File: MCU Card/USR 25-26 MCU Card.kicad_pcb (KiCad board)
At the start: 2 copper layers, 14 parts

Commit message: Update MCU card layout
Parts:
- removed D5, D6: LED, LED_SMD:LED_1206_3216Metric_Pad1.42x1.75mm_HandSolder
- removed R4, R5, R6: 220, Resistor_SMD:R_1206_3216Metric_Pad1.30x1.75mm_HandSolder
- added A2: RaspberryPi_Pico_W, Module:RaspberryPi_Pico_Common_THT, F.Cu at (119.4, 78.6)
- added U1: ~, USR:LSM6DSO, F.Cu at (161.7, 128.0)
- A1: footprint Module:RaspberryPi_Pico_W_SMD_HandSolder -> Module:RaspberryPi_Pico_Common_THT
- D1, D2, D3: footprint LED_SMD:LED_1206_3216Metric_Pad1.42x1.75mm_HandSolder -> LED_THT:LED_D3.0mm
- D4: value LED -> 1N5819; footprint LED_SMD:LED_1206_3216Metric_Pad1.42x1.75mm_HandSolder -> Diode_THT:D_DO-41_SOD81_P10.16mm_Horizontal
- R1, R2, R3: value 220 -> 510R; footprint Resistor_SMD:R_1206_3216Metric_Pad1.30x1.75mm_HandSolder -> Resistor_THT:R_Axial_DIN0207_L6.3mm_D2.5mm_P10.16mm_Horizontal
- moved J1 100.2 mm to (138.4, 144.6)
- moved D1 78.5 mm to (168.9, 101.4), turned to 90 degrees
- moved D2 70.6 mm to (168.9, 91.3), turned to 90 degrees
- moved D3 62.1 mm to (168.9, 81.1), turned to 90 degrees
- moved R1 51.8 mm to (152.4, 98.9)
- moved R2 39.7 mm to (152.4, 88.7)
- moved A1 29.9 mm to (61.0, 78.7)
- moved R3 28.7 mm to (152.4, 78.6)
- moved D4 23.8 mm to (88.9, 81.1)
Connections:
- A1 pad 1: Net-(A1-GPIO0) -> unconnected-(A1-GPIO0-Pad1)
- A1 pad 11: Net-(A1-GPIO8) -> unconnected-(A1-GPIO8-Pad11)
- A1 pad 21: Net-(A1-GPIO16) -> unconnected-(A1-GPIO16-Pad21)
- A1 pad 22: /SPI0_CS2 -> unconnected-(A1-GPIO17-Pad22)
- A1 pad 24: /M1_SLP -> unconnected-(A1-GPIO18-Pad24)
- A1 pad 25: /M2_SLP -> unconnected-(A1-GPIO19-Pad25)
- A1 pad 26: /M1_FLT -> unconnected-(A1-GPIO20-Pad26)
- A1 pad 27: /M2_FLT -> unconnected-(A1-GPIO21-Pad27)
- A1 pad 29: Net-(A1-GPIO22) -> unconnected-(A1-GPIO22-Pad29)
- A1 pad 39: +5V -> Net-(A1-VSYS)
- A1 pad 40: unconnected-(A1-VBUS-Pad40) -> VBUS
- D1 pad 1: Net-(D1-K) -> GND
- D1 pad 2: +5V -> Net-(D1-A)
- D2 pad 1: Net-(D2-K) -> GND
- D2 pad 2: +3V3 -> Net-(D2-A)
- D3 pad 1: Net-(D3-K) -> GND
- D3 pad 2: Net-(A1-GPIO0) -> Net-(D3-A)
- D4 pad 1: Net-(D4-K) -> Net-(A1-VSYS)
- D4 pad 2: Net-(A1-GPIO8) -> +5V
- J1 pad 32: +5V -> unconnected-(J1-Pad32)
- J1 pad 33: +3V3 -> unconnected-(J1-Pad33)
- J1 pad 34: GND -> unconnected-(J1-Pad34)
- J1 pad 35: /SPI0_MOSI -> unconnected-(J1-Pad35)
- J1 pad 36: /SPI0_MISO -> unconnected-(J1-Pad36)
- J1 pad 37: /SPI0_SCLK -> unconnected-(J1-Pad37)
- J1 pad 38: /SPI0_CS0 -> unconnected-(J1-Pad38)
- J1 pad 39: /SPI0_CS1 -> unconnected-(J1-Pad39)
- J1 pad 40: /SPI0_CS2 -> unconnected-(J1-Pad40)
- J1 pad 41: GND -> unconnected-(J1-Pad41)
- J1 pad 42: /SPI1_MOSI -> unconnected-(J1-Pad42)
- J1 pad 43: /SPI1_MISO -> unconnected-(J1-Pad43)
- J1 pad 44: /SPI1_SCLK -> unconnected-(J1-Pad44)
- J1 pad 45: /SPI1_CS0 -> unconnected-(J1-Pad45)
- J1 pad 46: /SPI1_CS1 -> unconnected-(J1-Pad46)
- J1 pad 47: GND -> unconnected-(J1-Pad47)
- J1 pad 48: /M1_DIR -> unconnected-(J1-Pad48)
- J1 pad 49: /M1_FLT -> unconnected-(J1-Pad49)
- J1 pad 50: /M1_PWM -> unconnected-(J1-Pad50)
- J1 pad 51: /M1_SLP -> unconnected-(J1-Pad51)
- J1 pad 52: GND -> unconnected-(J1-Pad52)
- J1 pad 53: /M2_DIR -> unconnected-(J1-Pad53)
- J1 pad 54: /M2_FLT -> unconnected-(J1-Pad54)
- J1 pad 55: /M2_PWM -> unconnected-(J1-Pad55)
- J1 pad 56: /M2_SLP -> unconnected-(J1-Pad56)
- R1 pad 1: Net-(D1-K) -> VBUS
- R1 pad 2: GND -> Net-(D1-A)
- R2 pad 1: Net-(D2-K) -> +5V
- R2 pad 2: GND -> Net-(D2-A)
- R3 pad 1: Net-(D6-K) -> +3V3
- R3 pad 2: GND -> Net-(D3-A)
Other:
- board outline added: 129.5 x 76.2 mm
- board text added: "3V3_OUT"
- board text added: ":)"
- board text added: "JG Vincent Banh MCU Card 25-26"
- board text added: "SEC_PWR"
- board text added: "USB_PWR"

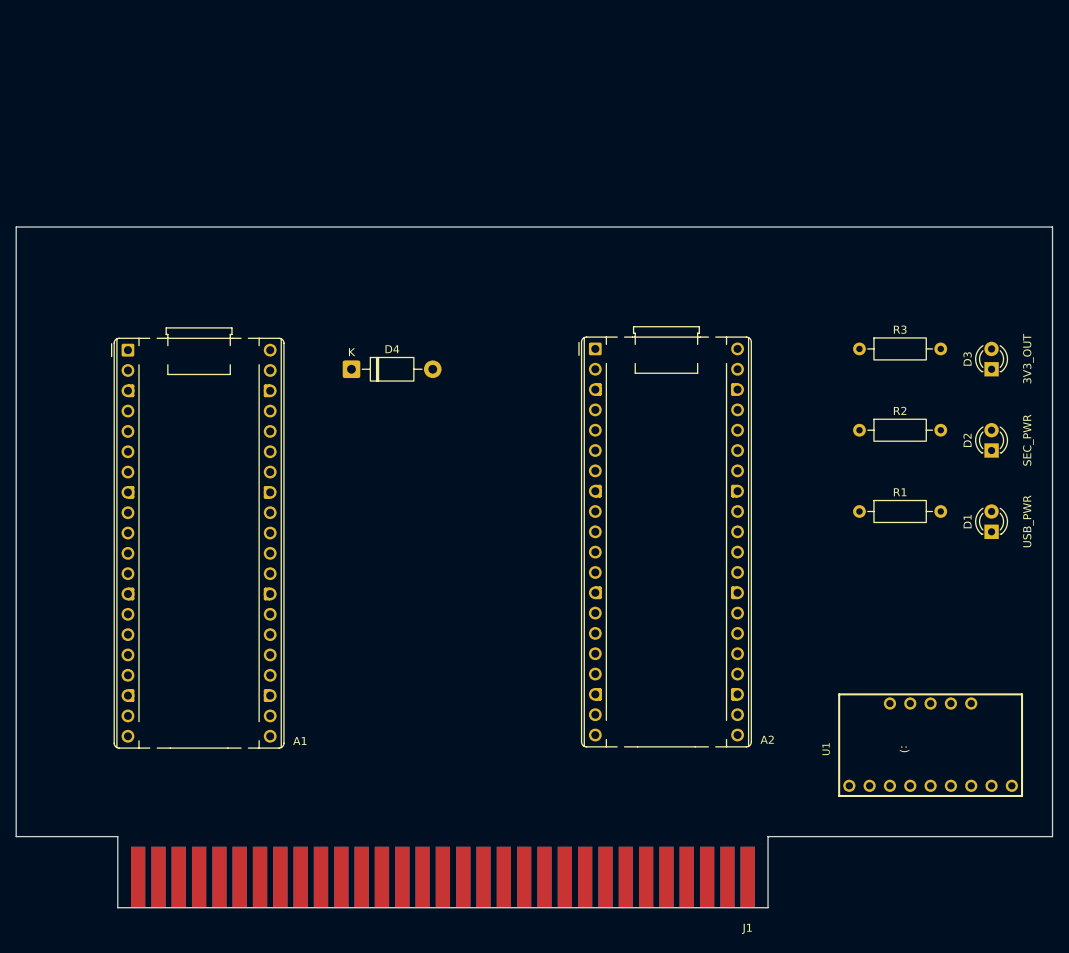
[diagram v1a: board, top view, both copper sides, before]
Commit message: updated MCU card
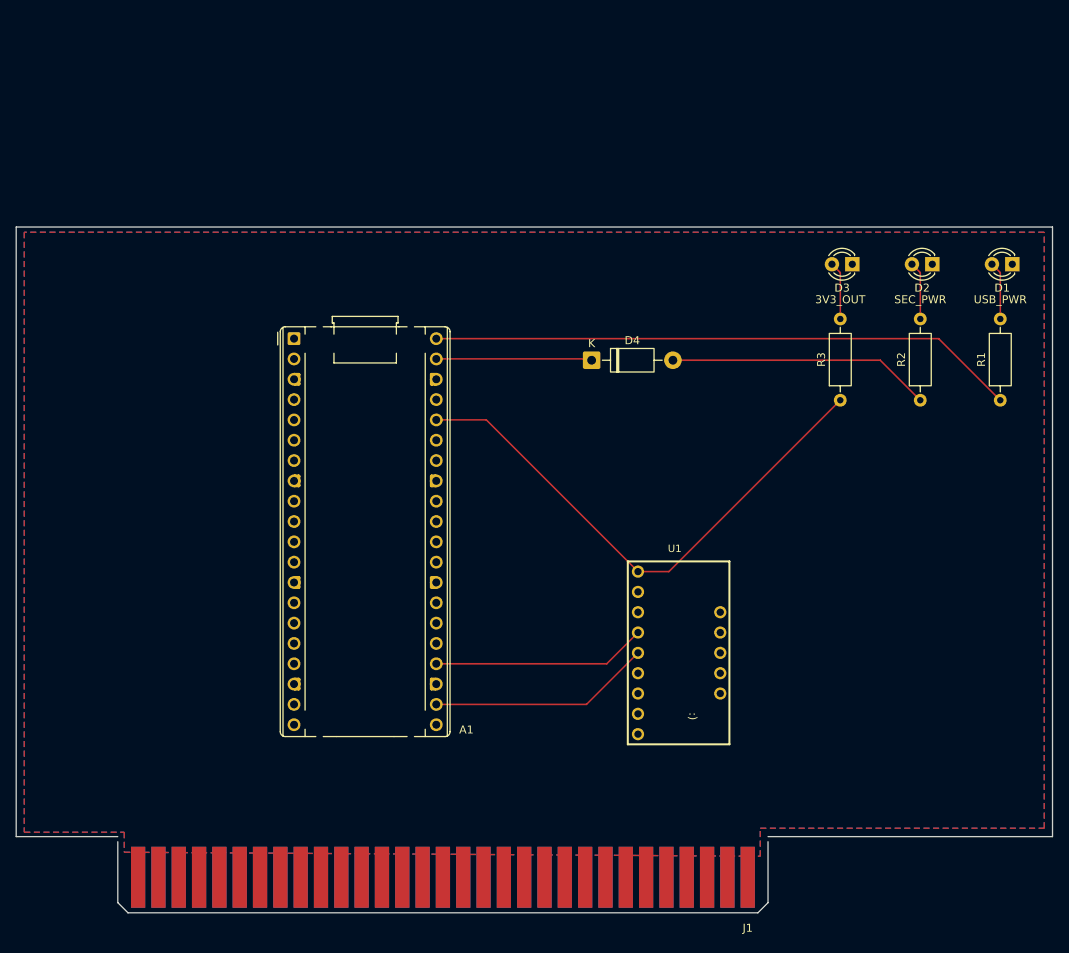
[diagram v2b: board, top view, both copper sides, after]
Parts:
- removed A2: RaspberryPi_Pico_W, Module:RaspberryPi_Pico_Common_THT
- moved U1 33.6 mm to (129.9, 117.0), turned to 0 degrees
- moved D1 33.5 mm to (171.5, 68.0), turned to 180 degrees
- moved D4 30.0 mm to (118.9, 80.0)
- moved D2 24.4 mm to (161.5, 68.0), turned to 180 degrees
- moved R1 22.4 mm to (170.0, 85.0), turned to 90 degrees
- moved D3 21.8 mm to (151.5, 68.0), turned to 180 degrees
- moved A1 20.8 mm to (81.7, 77.3)
- moved R2 8.47 mm to (160.0, 85.0), turned to 90 degrees
- moved R3 6.85 mm to (150.0, 85.0), turned to 90 degrees
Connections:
- A1 pad 1: unconnected-(A1-GPIO0-Pad1) -> /M1_DIR
- A1 pad 10: /M2_DIR -> /M4_PWM
- A1 pad 11: unconnected-(A1-GPIO8-Pad11) -> /M1_SLP
- A1 pad 12: /SPI1_CS0 -> /M2_SLP
- A1 pad 14: /SPI1_SCLK -> /M3_SLP
- A1 pad 15: /SPI1_MOSI -> /M4_SLP
- A1 pad 16: /SPI1_MISO -> /UART_TX_MICRO
- A1 pad 17: /SPI1_CS1 -> /UART_RX_MICRO
- A1 pad 19: /M1_PWM -> /M1_FLT
- A1 pad 2: /SPI0_CS0 -> /M1_PWM
- A1 pad 20: /M2_PWM -> /M2_FLT
- A1 pad 21: unconnected-(A1-GPIO16-Pad21) -> /M3_FLT
- A1 pad 22: unconnected-(A1-GPIO17-Pad22) -> /IMU_SCL
- A1 pad 24: unconnected-(A1-GPIO18-Pad24) -> /IMU_SDA
- A1 pad 25: unconnected-(A1-GPIO19-Pad25) -> /M4_FLT
- A1 pad 4: /SPI0_SCLK -> /M2_DIR
- A1 pad 5: /SPI0_MOSI -> /M2_PWM
- A1 pad 6: /SPI0_MISO -> /M3_DIR
- A1 pad 7: /SPI0_CS1 -> /M3_PWM
- A1 pad 9: /M1_DIR -> /M4_DIR
- J1 pad 1: unconnected-(J1-Pad1) -> /UART_TX_MICRO
- J1 pad 10: unconnected-(J1-Pad10) -> /M1_FLT
- J1 pad 11: unconnected-(J1-Pad11) -> /M1_SLP
- J1 pad 12: unconnected-(J1-Pad12) -> GND
- J1 pad 13: unconnected-(J1-Pad13) -> /M2_DIR
- J1 pad 14: unconnected-(J1-Pad14) -> /M2_PWM
- J1 pad 15: unconnected-(J1-Pad15) -> GND
- J1 pad 16: unconnected-(J1-Pad16) -> /M2_FLT
- J1 pad 17: unconnected-(J1-Pad17) -> /M2_SLP
- J1 pad 18: unconnected-(J1-Pad18) -> GND
- J1 pad 19: unconnected-(J1-Pad19) -> /M3_DIR
- J1 pad 2: unconnected-(J1-Pad2) -> /UART_RX_MICRO
- J1 pad 20: unconnected-(J1-Pad20) -> /M3_PWM
- J1 pad 21: unconnected-(J1-Pad21) -> GND
- J1 pad 22: unconnected-(J1-Pad22) -> /M3_FLT
- J1 pad 23: unconnected-(J1-Pad23) -> /M3_SLP
- J1 pad 24: unconnected-(J1-Pad24) -> GND
- J1 pad 25: unconnected-(J1-Pad25) -> /M4_DIR
- J1 pad 26: unconnected-(J1-Pad26) -> /M4_PWM
- J1 pad 27: unconnected-(J1-Pad27) -> GND
- J1 pad 28: unconnected-(J1-Pad28) -> /M4_FLT
- J1 pad 29: unconnected-(J1-Pad29) -> /M4_SLP
- J1 pad 3: unconnected-(J1-Pad3) -> GND
- J1 pad 30: unconnected-(J1-Pad30) -> GND
- J1 pad 31: unconnected-(J1-Pad31) -> +5V
- J1 pad 34: unconnected-(J1-Pad34) -> GND
- J1 pad 39: unconnected-(J1-Pad39) -> GND
- J1 pad 6: unconnected-(J1-Pad6) -> GND
- J1 pad 7: unconnected-(J1-Pad7) -> /M1_DIR
- J1 pad 8: unconnected-(J1-Pad8) -> /M1_PWM
- J1 pad 9: unconnected-(J1-Pad9) -> GND
- U1 pad 1: unconnected-(U1-VDD3V3_out-Pad1) -> +3V3
- U1 pad 10: unconnected-(U1-GND-Pad10) -> GND
- U1 pad 11: unconnected-(U1-SDx-Pad11) -> GND
- U1 pad 12: unconnected-(U1-SCx-Pad12) -> GND
- U1 pad 4: unconnected-(U1-SDA/SDI/SDO-Pad4) -> /IMU_SDA
- U1 pad 5: unconnected-(U1-SCL/SPC-Pad5) -> /IMU_SCL
- U1 pad 6: unconnected-(U1-SDO/SA0-Pad6) -> Net-(U1-SDO/SA0)
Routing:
- net VBUS: track 0.00 -> 73.7 mm
- net +3V3: track 0.00 -> 67.2 mm
- net +5V: track 0.00 -> 33.0 mm
- net /IMU_SCL: track 0.00 -> 27.9 mm
- net /IMU_SDA: track 0.00 -> 26.8 mm
- net Net-(A1-VSYS): track 0.00 -> 19.5 mm
- net Net-(D3-A): track 0.00 -> 7.27 mm
- net Net-(D2-A): track 0.00 -> 7.27 mm
- net Net-(D1-A): track 0.00 -> 7.27 mm
- net unconnected-(J1-Pad54): track 0.00 -> 2.92 mm
- added copper zone on B.Cu, net GND
- added copper zone on F.Cu, net GND

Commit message: Finished traces for the MCU card PCB
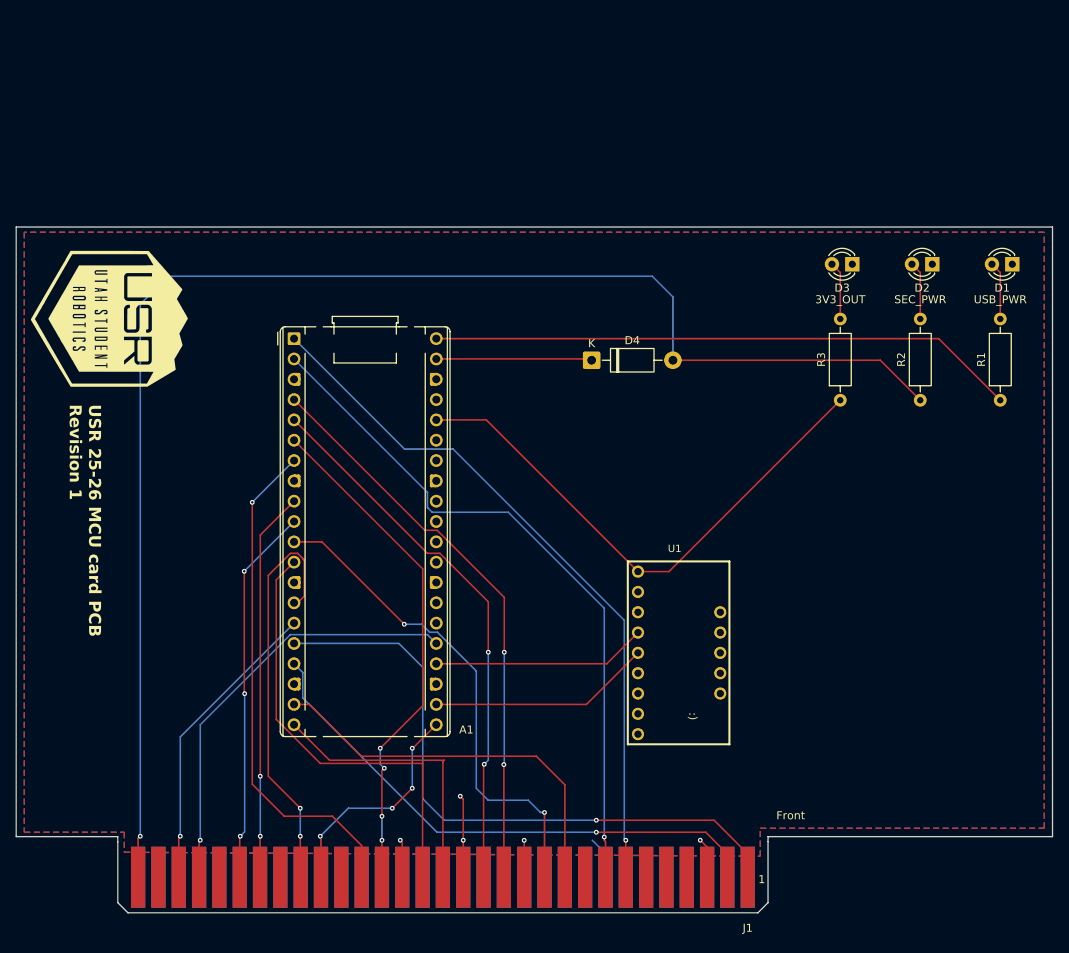
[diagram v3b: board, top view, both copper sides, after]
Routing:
- net +5V: track 33.0 -> 181.7 mm, vias 0 -> 1
- net /M1_DIR: track 0.00 -> 88.1 mm, vias 0 -> 1
- net /M1_PWM: track 0.00 -> 86.5 mm, vias 0 -> 1
- net /UART_TX_MICRO: track 0.00 -> 80.1 mm, vias 0 -> 1
- net /M2_DIR: track 0.00 -> 71.5 mm, vias 0 -> 2
- net /UART_RX_MICRO: track 0.00 -> 68.8 mm, vias 0 -> 1
- net /M2_PWM: track 0.00 -> 68.4 mm, vias 0 -> 2
- net /M3_DIR: track 0.00 -> 63.8 mm, vias 0 -> 4
- net /M3_PWM: track 0.00 -> 63.4 mm, vias 0 -> 1
- net /M1_SLP: track 0.00 -> 62.0 mm, vias 0 -> 2
- net /M2_SLP: track 0.00 -> 55.4 mm
- net /M4_FLT: track 0.00 -> 53.7 mm, vias 0 -> 1
- net /M3_SLP: track 0.00 -> 51.5 mm, vias 0 -> 2
- net /M1_FLT: track 0.00 -> 49.6 mm
- net /M4_DIR: track 0.00 -> 48.8 mm, vias 0 -> 2
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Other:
- board size 129.5 x 76.2 mm -> 129.5 x 76.8 mm
- board text added: "1"
- board text added: "Front"
- board text added: "Peter Burt JG Vincent Banh MCU Card 25-26"
- board text added: "USR 25-26 MCU card PCB Revision 1"
- board text removed: "JG Vincent Banh MCU Card 25-26"

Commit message: Fixed trace errors on MCU board
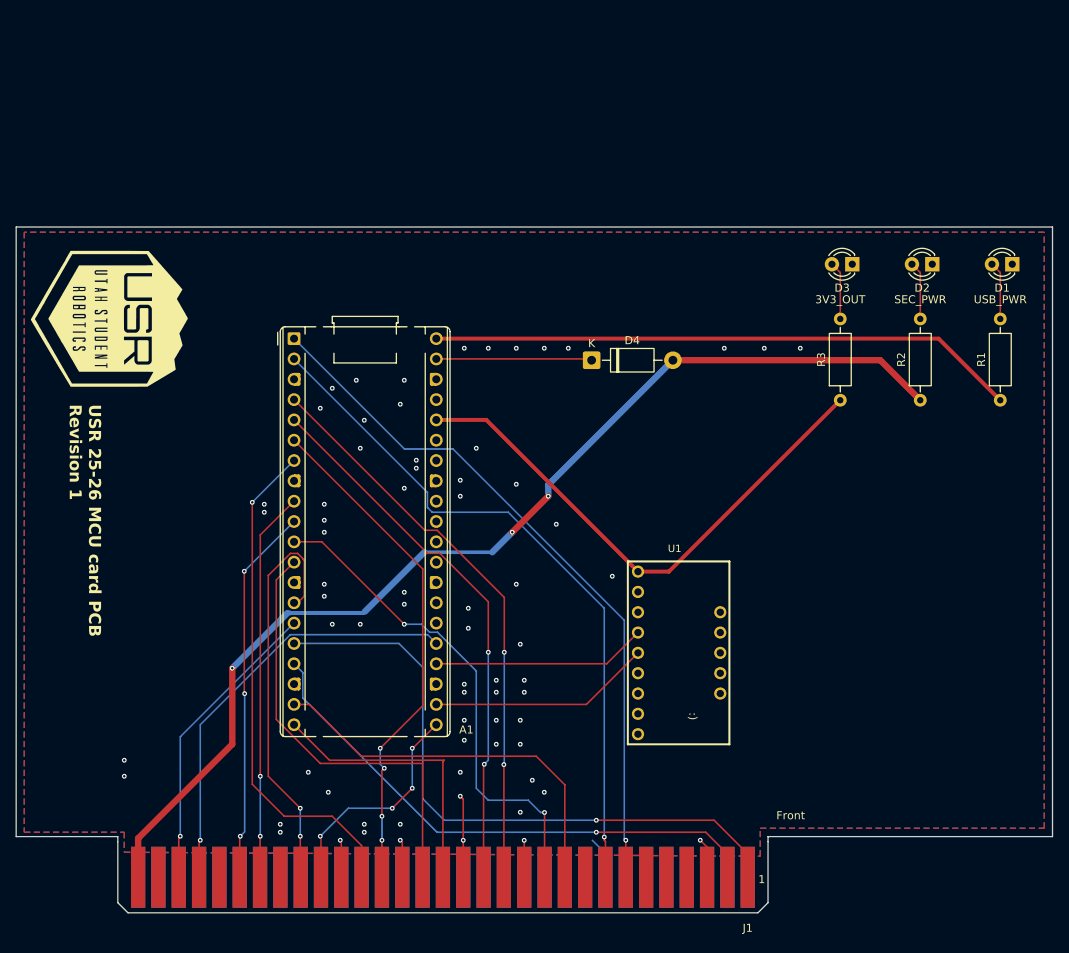
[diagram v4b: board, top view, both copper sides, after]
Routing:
- net +5V: track 181.7 -> 135.9 mm, vias 1 -> 3
- net GND: track 29.9 -> 34.6 mm, vias 5 -> 70
